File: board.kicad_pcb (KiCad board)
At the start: 2 copper layers, 10 parts, among them IC1 ATTINY85-P, P1 USB_OTG, P2 CONN_01X04, P3 CONN_01X04, P4 USBasp, SW1 SW_PUSH

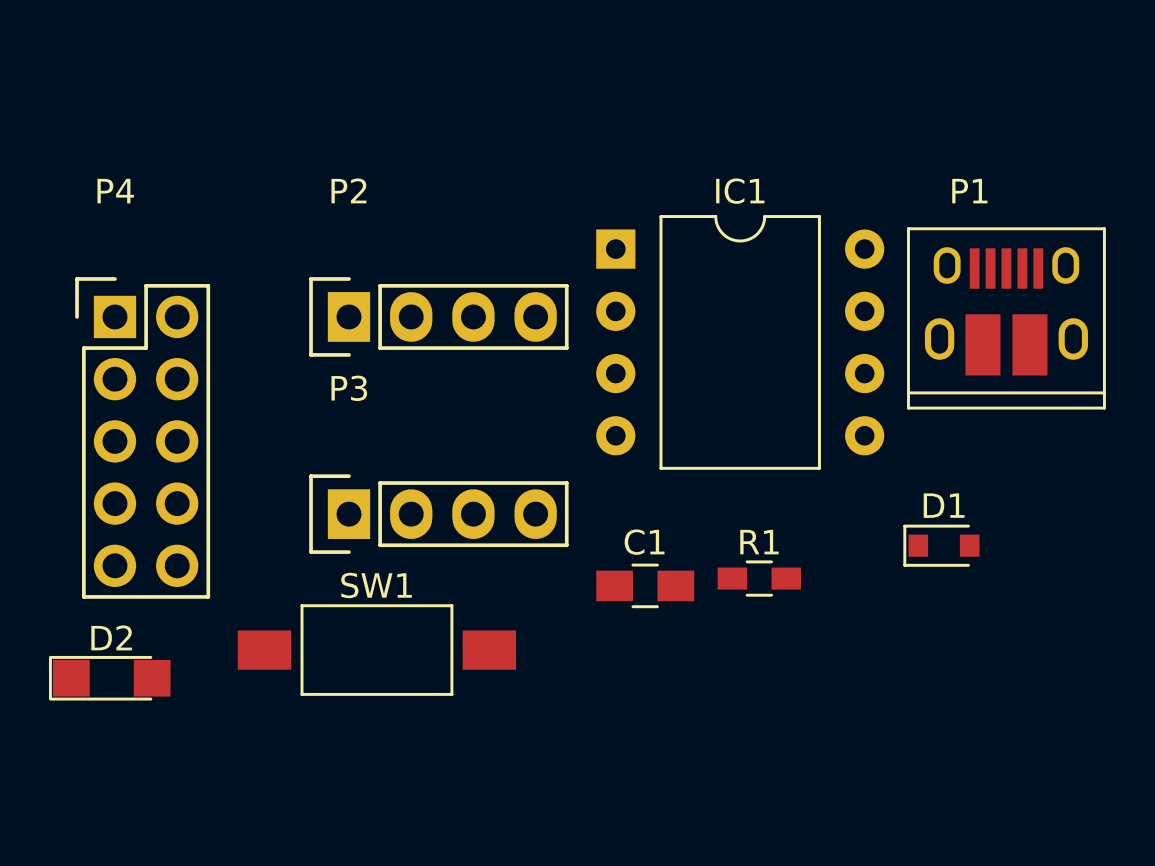
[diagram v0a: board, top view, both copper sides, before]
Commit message: Connect push button
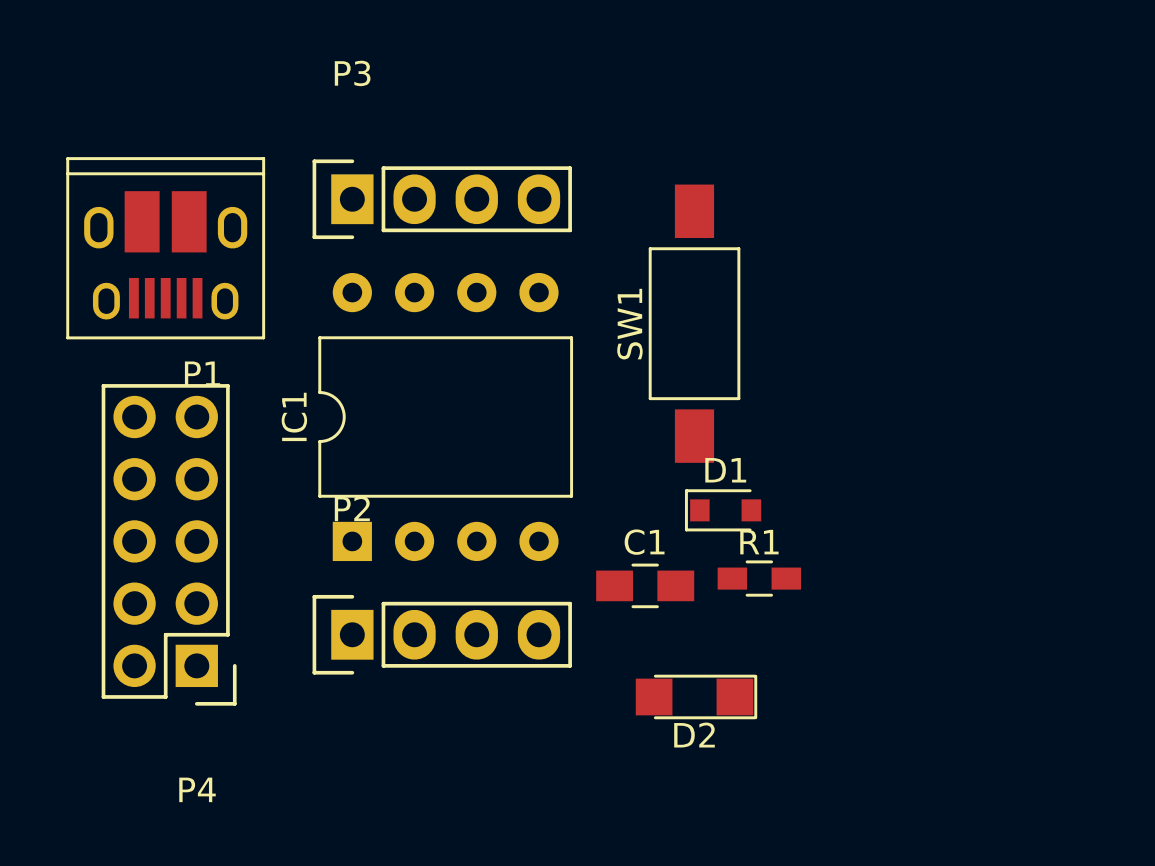
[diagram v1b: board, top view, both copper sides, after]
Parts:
- moved P1 34.4 mm to (135.9, 139.7), turned to 180 degrees
- moved D2 23.8 mm to (157.5, 157.5), turned to 180 degrees
- moved SW1 18.6 mm to (157.5, 142.2), turned to 90 degrees
- moved IC1 16.1 mm to (143.5, 151.1), turned to 90 degrees
- moved P4 14.6 mm to (137.2, 156.2), turned to 180 degrees
- moved P2 13.0 mm to (143.5, 154.9)
- moved P3 12.9 mm to (143.5, 137.2)
- moved D1 9.03 mm to (158.8, 149.9)
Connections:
- SW1 pad 1: Net-(SW1-Pad1) -> Net-(D1-Pad1)
- SW1 pad 2: Net-(SW1-Pad2) -> GND

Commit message: Add some routing
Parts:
- P1: value USB_OTG -> (none)
- P2, P3: value CONN_01X04 -> (none)
- SW1: value SW_PUSH -> (none)
- moved D2 2.54 mm to (157.5, 154.9)
- moved C1 1.89 mm to (154.9, 151.1), turned to 90 degrees
- moved D1 1.80 mm to (157.5, 151.1), turned to 270 degrees
- moved R1 1.52 mm to (160.0, 151.1), turned to 270 degrees
- moved P1 1.27 mm to (137.2, 139.7), turned to 270 degrees
- moved P4 1.27 mm to (138.4, 156.2)
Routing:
- net +5V: track 0.00 -> 61.1 mm, vias 0 -> 2
- net /PB0: track 0.00 -> 28.4 mm
- net /PB5: track 0.00 -> 27.1 mm, vias 0 -> 3
- net /PB1: track 0.00 -> 17.6 mm
- net /PB2: track 0.00 -> 16.1 mm, vias 0 -> 2
- net Net-(D1-Pad1): track 0.00 -> 5.81 mm
- net GND: track 0.00 -> 3.81 mm
- net /PB4: track 0.00 -> 3.81 mm
- net /PB3: track 0.00 -> 3.81 mm
- net Net-(D2-Pad1): track 0.00 -> 3.08 mm
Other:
- board outline added: 27.9 x 23.5 mm
- board text added: "attiny programmer v1.0"

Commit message: Add GND and VCC covers
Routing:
- net +5V: track 61.1 -> 1.65 mm, vias 2 -> 0
- added copper zone on B.Cu, net +5V
- added copper zone on F.Cu, net GND
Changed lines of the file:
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@@
   (general
     (links 33)
-    (no_connects 13)
+    (no_connects 5)
     (area 133.274999 135.179999 161.365001 158.825001)
     (thickness 1.6)
     (drawings 5)
-    (tracks 66)
+    (tracks 47)
     (zones 0)
     (modules 10)
@@
   (gr_line (start 133.35 158.75) (end 161.29 158.75) (angle 90) (layer Edge.Cuts) (width 0.15))
   (gr_line (start 133.35 135.255) (end 133.35 158.75) (angle 90) (layer Edge.Cuts) (width 0.15))
-  (segment (start 143.51 137.16) (end 143.51 140.97) (width 0.25) (layer F.Cu) (net 1) (status C00000))
-  (segment (start 135.89 156.21) (end 135.255 156.21) (width 0.25) (layer F.Cu) (net 1) (status C00000))
-  (segment (start 135.255 156.21) (end 133.985 154.94) (width 0.25) (layer F.Cu) (net 1) (status 400000))
-  (segment (start 139.67 138.4) (end 138.66 138.4) (width 0.25) (layer F.Cu) (net 1) (status 800000))
-  (segment (start 140.97 139.7) (end 139.67 138.4) (width 0.25) (layer F.Cu) (net 1))
-  (via (at 140.97 139.7) (size 0.6) (drill 0.4) (layers F.Cu B.Cu) (net 1))
-  (segment (start 140.97 146.05) (end 140.97 139.7) (width 0.25) (layer B.Cu) (net 1))
-  (segment (start 139.7 147.32) (end 140.97 146.05) (width 0.25) (layer B.Cu) (net 1))
-  (via (at 139.7 147.32) (size 0.6) (drill 0.4) (layers F.Cu B.Cu) (net 1))
-  (segment (start 134.62 147.32) (end 139.7 147.32) (width 0.25) (layer F.Cu) (net 1))
-  (segment (start 133.985 147.955) (end 134.62 147.32) (width 0.25) (layer F.Cu) (net 1))
-  (segment (start 133.985 154.94) (end 133.985 147.955) (width 0.25) (layer F.Cu) (net 1))
-  (segment (start 138.66 138.4) (end 140.94 138.4) (width 0.25) (layer F.Cu) (net 1))
-  (segment (start 142.18 137.16) (end 143.51 137.16) (width 0.25) (layer F.Cu) (net 1))
-  (segment (start 140.94 138.4) (end 142.18 137.16) (width 0.25) (layer F.Cu) (net 1))
+  (segment (start 135.89 156.21) (end 135.255 156.21) (width 0.25) (layer F.Cu) (net 1))
   (segment (start 135.89 156.21) (end 135.89 156.845) (width 0.25) (layer F.Cu) (net 1))
-  (segment (start 135.89 156.845) (end 137.16 158.115) (width 0.25) (layer F.Cu) (net 1))
-  (segment (start 137.16 158.115) (end 153.035 158.115) (width 0.25) (layer F.Cu) (net 1))
-  (segment (start 153.035 158.115) (end 155.83 155.32) (width 0.25) (layer F.Cu) (net 1))
   (segment (start 155.83 155.32) (end 155.83 154.94) (width 0.25) (layer F.Cu) (net 1))
-  (segment (start 154.94 152.38) (end 154.94 154.05) (width 0.25) (layer F.Cu) (net 1))
-  (segment (start 154.94 154.05) (end 155.83 154.94) (width 0.25) (layer F.Cu) (net 1))
   (segment (start 151.13 151.13) (end 151.13 154.94) (width 0.25) (layer F.Cu) (net 2))
   (segment (start 157.48 146.83) (end 157.48 150.08) (width 0.25) (layer F.Cu) (net 3))
   (segment (start 157.48 150.08) (end 159.97 150.08) (width 0.25) (layer F.Cu) (net 3))
   (segment (start 159.97 150.08) (end 160.02 150.03) (width 0.25) (layer F.Cu) (net 3))
-  (segment (start 143.51 151.13) (end 143.51 149.225) (width 0.25) (layer F.Cu) (net 4) (status 400000))
-  (segment (start 156.43 152.18) (end 157.48 152.18) (width 0.25) (layer F.Cu) (net 4) (status 800000))
+  (segment (start 143.51 151.13) (end 143.51 149.225) (width 0.25) (layer F.Cu) (net 4))
+  (segment (start 156.43 152.18) (end 157.48 152.18) (width 0.25) (layer F.Cu) (net 4))
   (segment (start 156.21 152.4) (end 156.43 152.18) (width 0.25) (layer F.Cu) (net 4))
   (via (at 156.21 152.4) (size 0.6) (drill 0.4) (layers F.Cu B.Cu) (net 4))
@@
   (segment (start 144.145 148.59) (end 151.765 148.59) (width 0.25) (layer F.Cu) (net 4))
   (segment (start 143.51 149.225) (end 144.145 148.59) (width 0.25) (layer F.Cu) (net 4))
-  (segment (start 138.43 151.13) (end 140.335 151.13) (width 0.25) (layer F.Cu) (net 4) (status 400000))
-  (segment (start 140.335 151.13) (end 143.51 151.13) (width 0.25) (layer B.Cu) (net 4) (status 800000))
+  (segment (start 138.43 151.13) (end 140.335 151.13) (width 0.25) (layer F.Cu) (net 4))
+  (segment (start 140.335 151.13) (end 143.51 151.13) (width 0.25) (layer B.Cu) (net 4))
   (via (at 140.335 151.13) (size 0.6) (drill 0.4) (layers F.Cu B.Cu) (net 4))
   (segment (start 143.51 151.13) (end 143.51 154.94) (width 0.25) (layer F.Cu) (net 4))
@@
   (segment (start 140.97 148.59) (end 142.24 147.32) (width 0.25) (layer F.Cu) (net 10))
   (segment (start 146.05 137.16) (end 146.05 140.97) (width 0.25) (layer F.Cu) (net 10))
+  (zone (net 1) (net_name +5V) (layer B.Cu) (hatch edge 0.508)
+    (connect_pads (clearance 0.508))
+    (min_thickness 0.254)
+    (fill yes (arc_segments 16) (thermal_gap 0.508) (thermal_bridge_width 0.508))
+    (polygon
+      (pts
+        (xy 161.29 158.75) (xy 133.35 158.75) (xy 133.35 135.255) (xy 161.29 135.255)
+      )
+    )
+  )
+  (zone (net 2) (net_name GND) (layer F.Cu) (hatch edge 0.508)
+    (connect_pads (clearance 0.508))
+    (min_thickness 0.254)
+    (fill yes (arc_segments 16) (thermal_gap 0.508) (thermal_bridge_width 0.508))
+    (polygon
+      (pts
+        (xy 161.29 158.75) (xy 133.35 158.75) (xy 133.35 135.255) (xy 161.29 135.255)
+      )
+    )
+  )
 )

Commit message: Update
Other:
- board text added: "attiny devboard"
- board text added: "github.com/alejandrogallo/attiny85_board"
- board text added: "v1.0"
- board text removed: "attiny programmer v1.0"
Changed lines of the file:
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@@
     (area 133.274999 135.179999 161.365001 158.825001)
     (thickness 1.6)
-    (drawings 5)
+    (drawings 7)
     (tracks 47)
     (zones 0)
@@
     (pad_to_mask_clearance 0.2)
     (aux_axis_origin 0 0)
-    (visible_elements FFFFFF7F)
+    (visible_elements FFFEFF7F)
     (pcbplotparams
       (layerselection 0x00030_80000001)
@@
     (tags "USB USB_B USB_micro USB_OTG")
     (attr smd)
-    (fp_text reference P1 (at -2.54 -16.51 360) (layer F.SilkS)
+    (fp_text reference P1 (at -2.54 -16.51 450) (layer F.SilkS)
       (effects (font (size 1 1) (thickness 0.15)))
     )
@@
     (descr "Through hole socket strip")
     (tags "socket strip")
-    (fp_text reference P2 (at 0 -5.1) (layer F.SilkS)
+    (fp_text reference P2 (at -2.54 0 90) (layer F.SilkS)
       (effects (font (size 1 1) (thickness 0.15)))
     )
@@
     (descr "Through hole socket strip")
     (tags "socket strip")
-    (fp_text reference P3 (at 0 -5.1) (layer F.SilkS)
+    (fp_text reference P3 (at 0 -5.1) (layer F.SilkS) hide
       (effects (font (size 1 1) (thickness 0.15)))
     )
@@
     (descr "Through hole pin header")
     (tags "pin header")
-    (fp_text reference P4 (at 0 -5.1 180) (layer F.SilkS)
+    (fp_text reference P4 (at 0 -5.1 180) (layer F.SilkS) hide
       (effects (font (size 1 1) (thickness 0.15)))
     )
@@
     )
   )
-  (gr_text "attiny programmer v1.0\n" (at 150.495 157.48) (layer F.SilkS)
+  (gr_text v1.0 (at 154.305 146.685 90) (layer F.SilkS)
     (effects (font (size 1 1) (thickness 0.25)))
   )
+  (gr_text "github.com/alejandrogallo/attiny85_board\n" (at 150.495 157.48) (layer F.SilkS)
+    (effects (font (size 0.6 0.6) (thickness 0.1)))
+  )
+  (gr_text "attiny devboard\n" (at 140.97 146.05 90) (layer F.SilkS)
+    (effects (font (size 1 1) (thickness 0.25)))
+  )
